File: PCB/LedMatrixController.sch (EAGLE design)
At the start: 17 parts, among them IC1 AT90S2313S, IC2 74LS595D

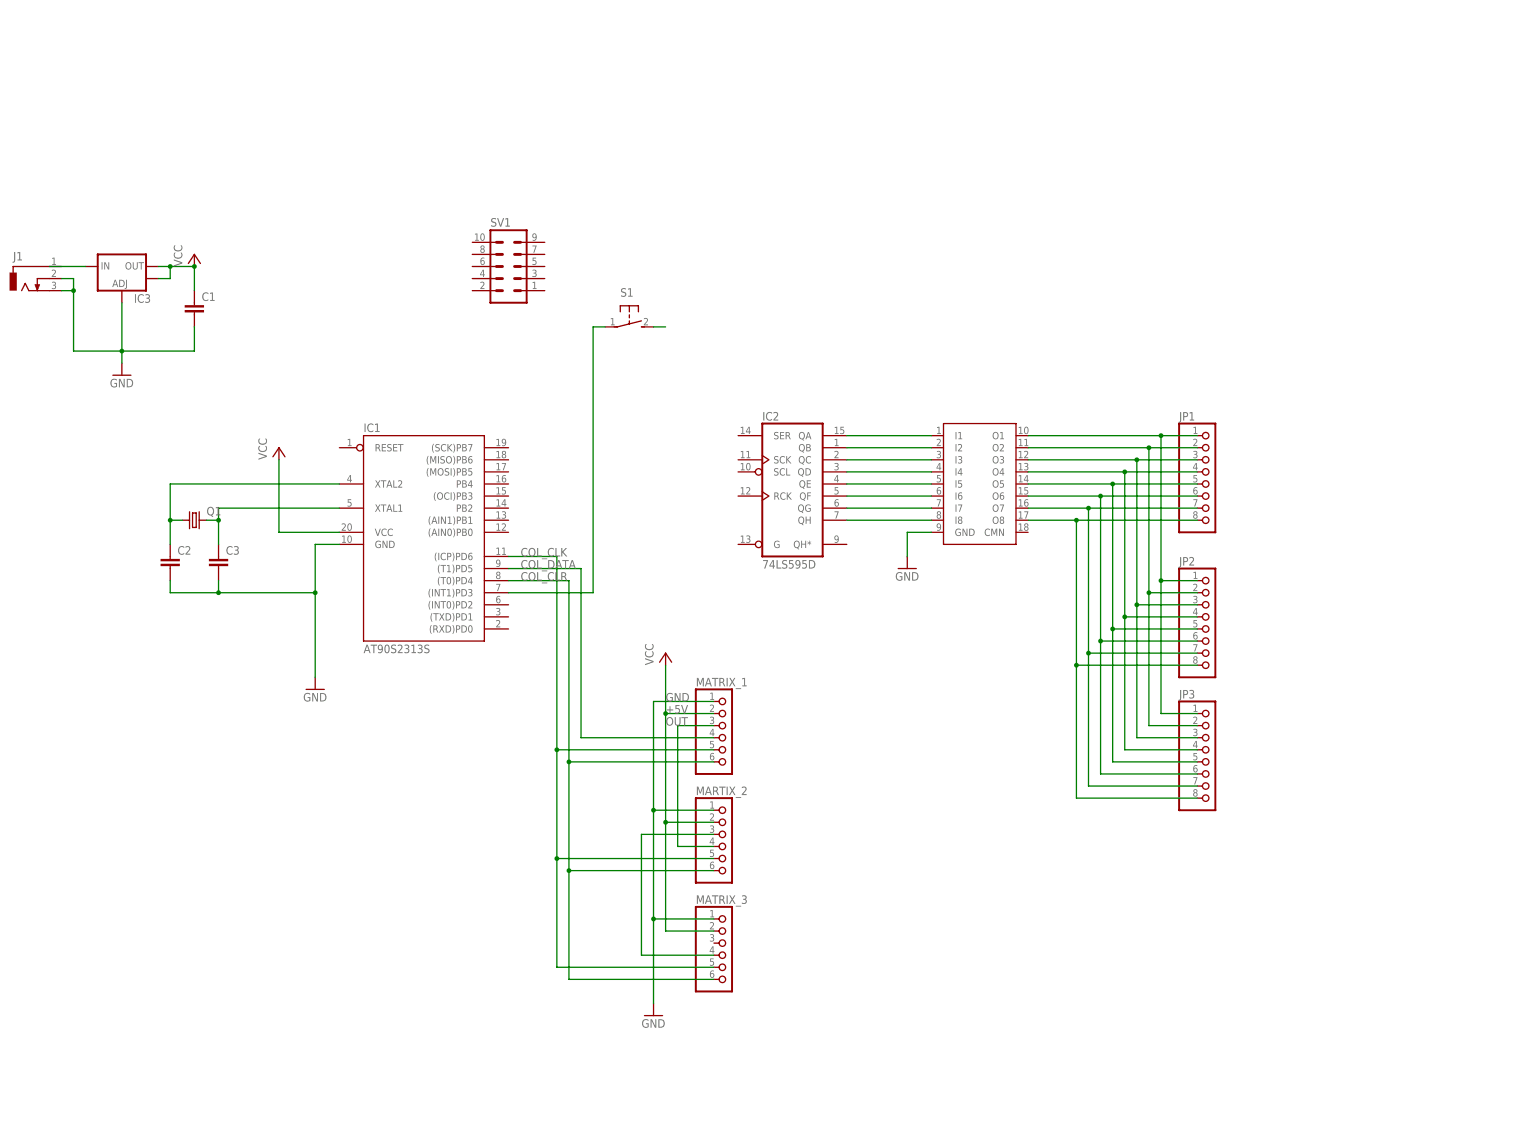
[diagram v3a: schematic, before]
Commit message: Improvments in the top layer of matrix controller pcb. Added eeprom, connected power source and almost all IC.
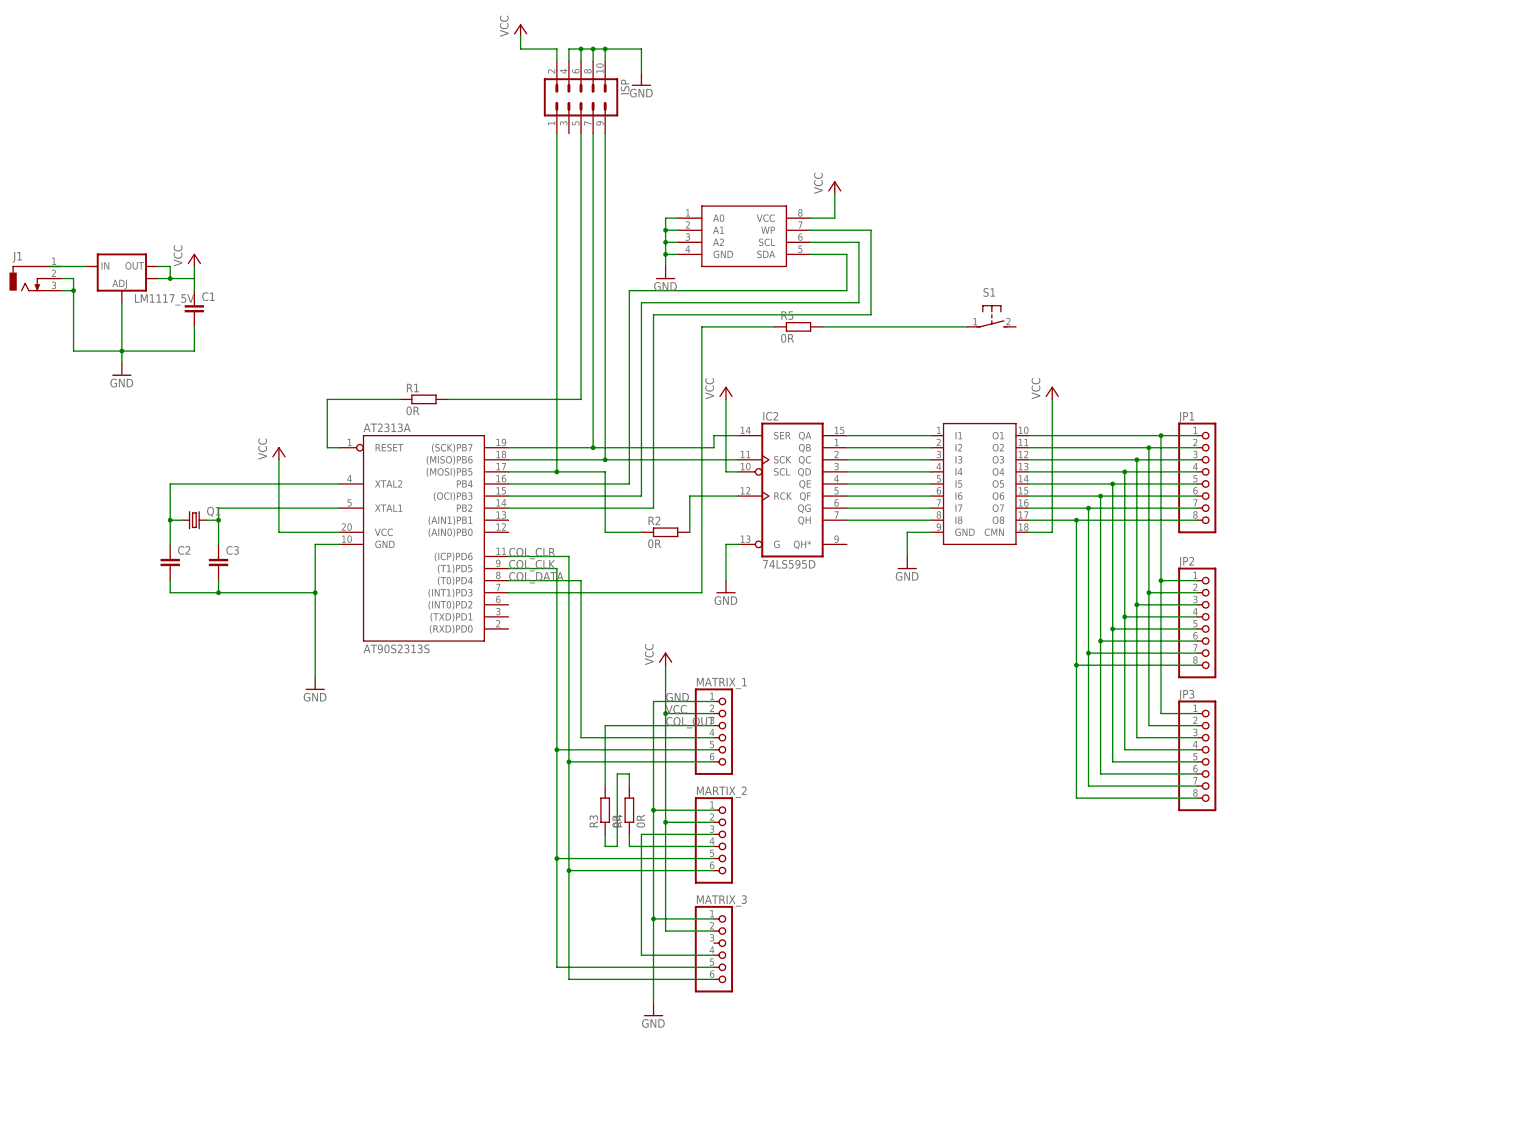
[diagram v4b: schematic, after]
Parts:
- removed SV1: (no value), con-ml:ML10
- added EEPROM: AT24C08, MJ:AT24C08
- added ISP: (no value), con-ml:ML10
- added R1, R2, R3, R4, R5: 0R, resistor:R-EU_R1206
- renumbered IC1 to AT2313A, IC3 to LM1117_5V
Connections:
- removed net +5V: AT2313A.VCC, C1.1, LM1117_5V.OUT, LM1117_5V.OUT@1, MARTIX_2.2, MATRIX_1.2, MATRIX_3.2
- removed net OUT: MARTIX_2.4, MATRIX_1.3
- new net COL_OUT: MATRIX_1.3, R3.2
- new net N$10: AT2313A.(OCI)PB3, EEPROM.SCL
- new net N$11: R3.1, R4.2
- new net N$12: AT2313A.PB2, EEPROM.WP
- new net N$13: AT2313A.RESET, R1.1
- new net N$14: R5.2, S1.P
- new net N$6: AT2313A.PB4, EEPROM.SDA
- new net N$7: MARTIX_2.4, R4.1
- new net N$9: ISP.5, R1.2
- new net ROW_LATCH: AT2313A.(MOSI)PB5, ISP.1, R2.1
- new net ROW_SCK: AT2313A.(MISO)PB6, IC2A.SCK, ISP.9
- new net ROW_SERIAL_DATA: AT2313A.(SCK)PB7, IC2A.SER, ISP.7
- new net VCC: AT2313A.VCC, C1.1, EEPROM.VCC, IC2A.SCL, ISP.2, LM1117_5V.OUT, LM1117_5V.OUT@1, MARTIX_2.2, MATRIX_1.2, MATRIX_3.2, U$1.CMN
- net COL_CLK: now also AT2313A.(T1)PD5; no longer AT2313A.(ICP)PD6
- net COL_CLR: now also AT2313A.(ICP)PD6; no longer AT2313A.(T0)PD4
- net COL_DATA: now also AT2313A.(T0)PD4; no longer AT2313A.(T1)PD5
- net GND: now also EEPROM.A0, EEPROM.A1, EEPROM.A2, EEPROM.GND, IC2A.G, ISP.10, ISP.4, ISP.6, ISP.8
- net N$4: now also R5.1; no longer S1.P
- net N$5: now also IC2A.RCK, R2.2; no longer S1.S
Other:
- moved on the sheet: S1

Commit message: Added usb connector, and power led.
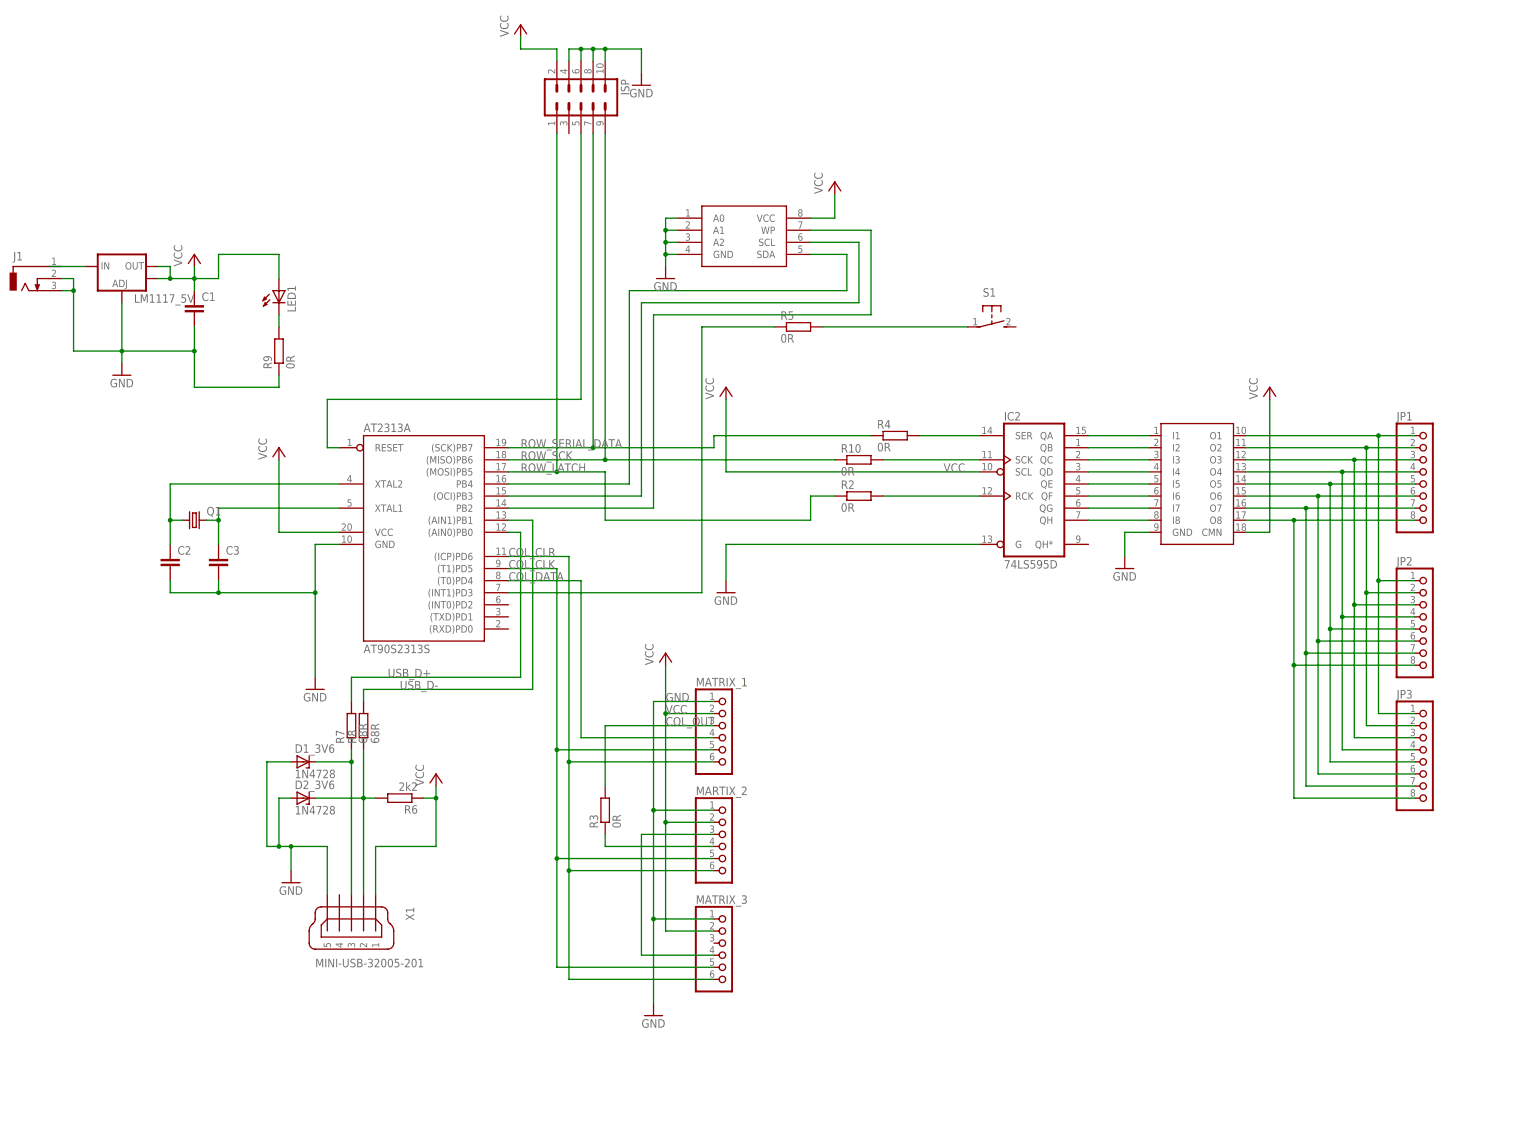
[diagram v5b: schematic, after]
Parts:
- removed R1: 0R, resistor:R-EU_R1206
- added D1_3V6, D2_3V6: 1N4728, diode:1N4728
- added LED1: (no value), led:LEDCHIPLED_1206
- added R10, R9: 0R, resistor:R-EU_R1206
- added R6: 2k2, resistor:R-EU_R1206
- added R7, R8: 68R, resistor:R-EU_R1206
- added X1: MINI-USB-32005-201, con-cypressindustries:MINI-USB-32005-201
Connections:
- removed net N$9: ISP.5, R1.2
- new net COL_OUT_2: MARTIX_2.4, R3.1
- new net N$17: LED1.C, R9.2
- new net USB_D+: AT2313A.(AIN0)PB0, R7.2
- new net USB_D-: AT2313A.(AIN1)PB1, R8.2
- new net USB_DATA+: D1_3V6.C, R7.1, X1.3
- new net USB_DATA-: D2_3V6.C, R6.2, R8.1, X1.2
- net GND: now also D1_3V6.A, D2_3V6.A, R9.1, X1.5
- net N$11: now also IC2A.SCK, R10.2; no longer R3.1, R4.2
- net N$13: now also ISP.5; no longer R1.1
- net N$7: now also IC2A.SER, R4.2; no longer MARTIX_2.4, R4.1
- net ROW_SCK: now also R10.1; no longer IC2A.SCK
- net ROW_SERIAL_DATA: now also R4.1; no longer IC2A.SER
- net VCC: now also LED1.A, R6.1, X1.1
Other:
- moved on the sheet: IC2, JP1, JP2, JP3, R2, R4
